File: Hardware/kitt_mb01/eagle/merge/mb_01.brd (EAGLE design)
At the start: 160 x 100 mm, 98 parts, among them CON1 ARDUINO_UNO, IC1.01 RT8293A, IC2.00 BQ24266RGET, IC3.01 LSM9DS1, P2 S2B-PH-K-S(LF)(SN), U6.01 TPS61032RSARPSDO-G16

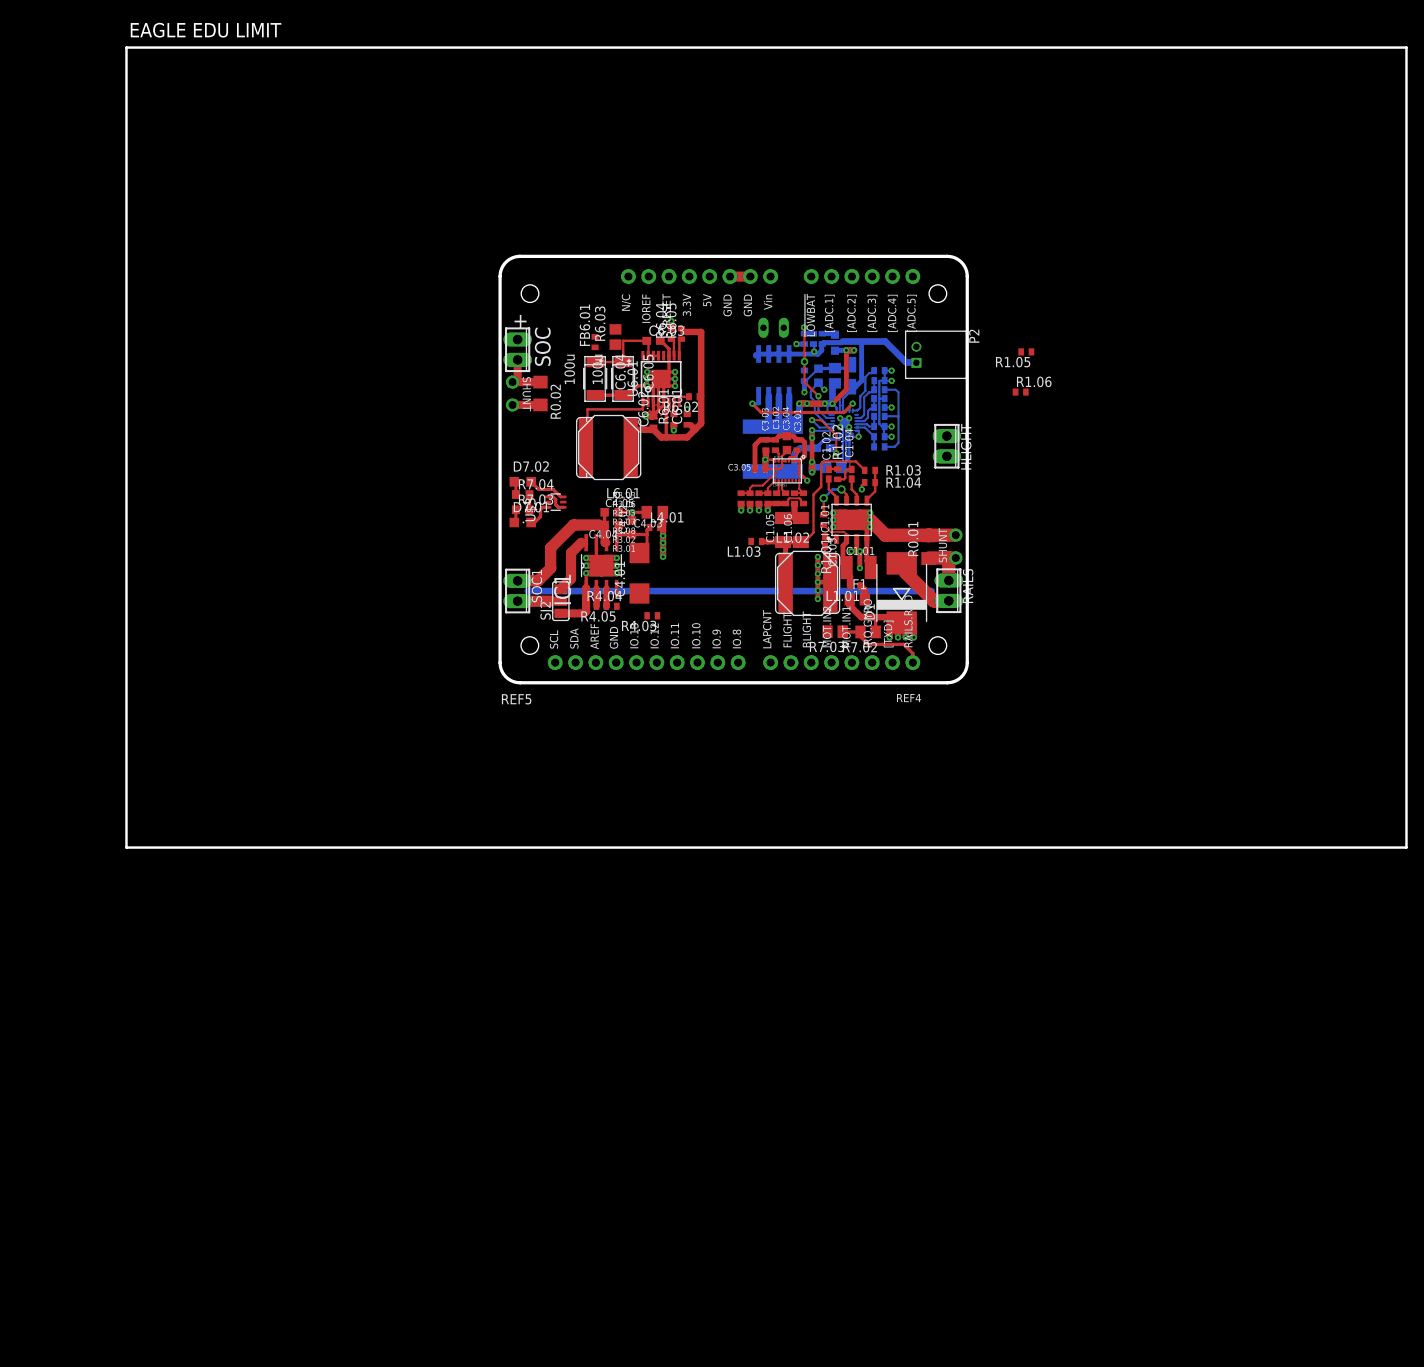
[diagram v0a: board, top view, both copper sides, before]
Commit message: snapshot of board merge
a point about the flipped LEDs with a hole:
it's mounted in reverse with a hole as a makeshift lightguard,
...because maybe.
There are actual LEDs with an lens attached (see knightbright),
but regular ones work as well obviously.
Also it allows for text to be silk'd right next to it, which is sweet.
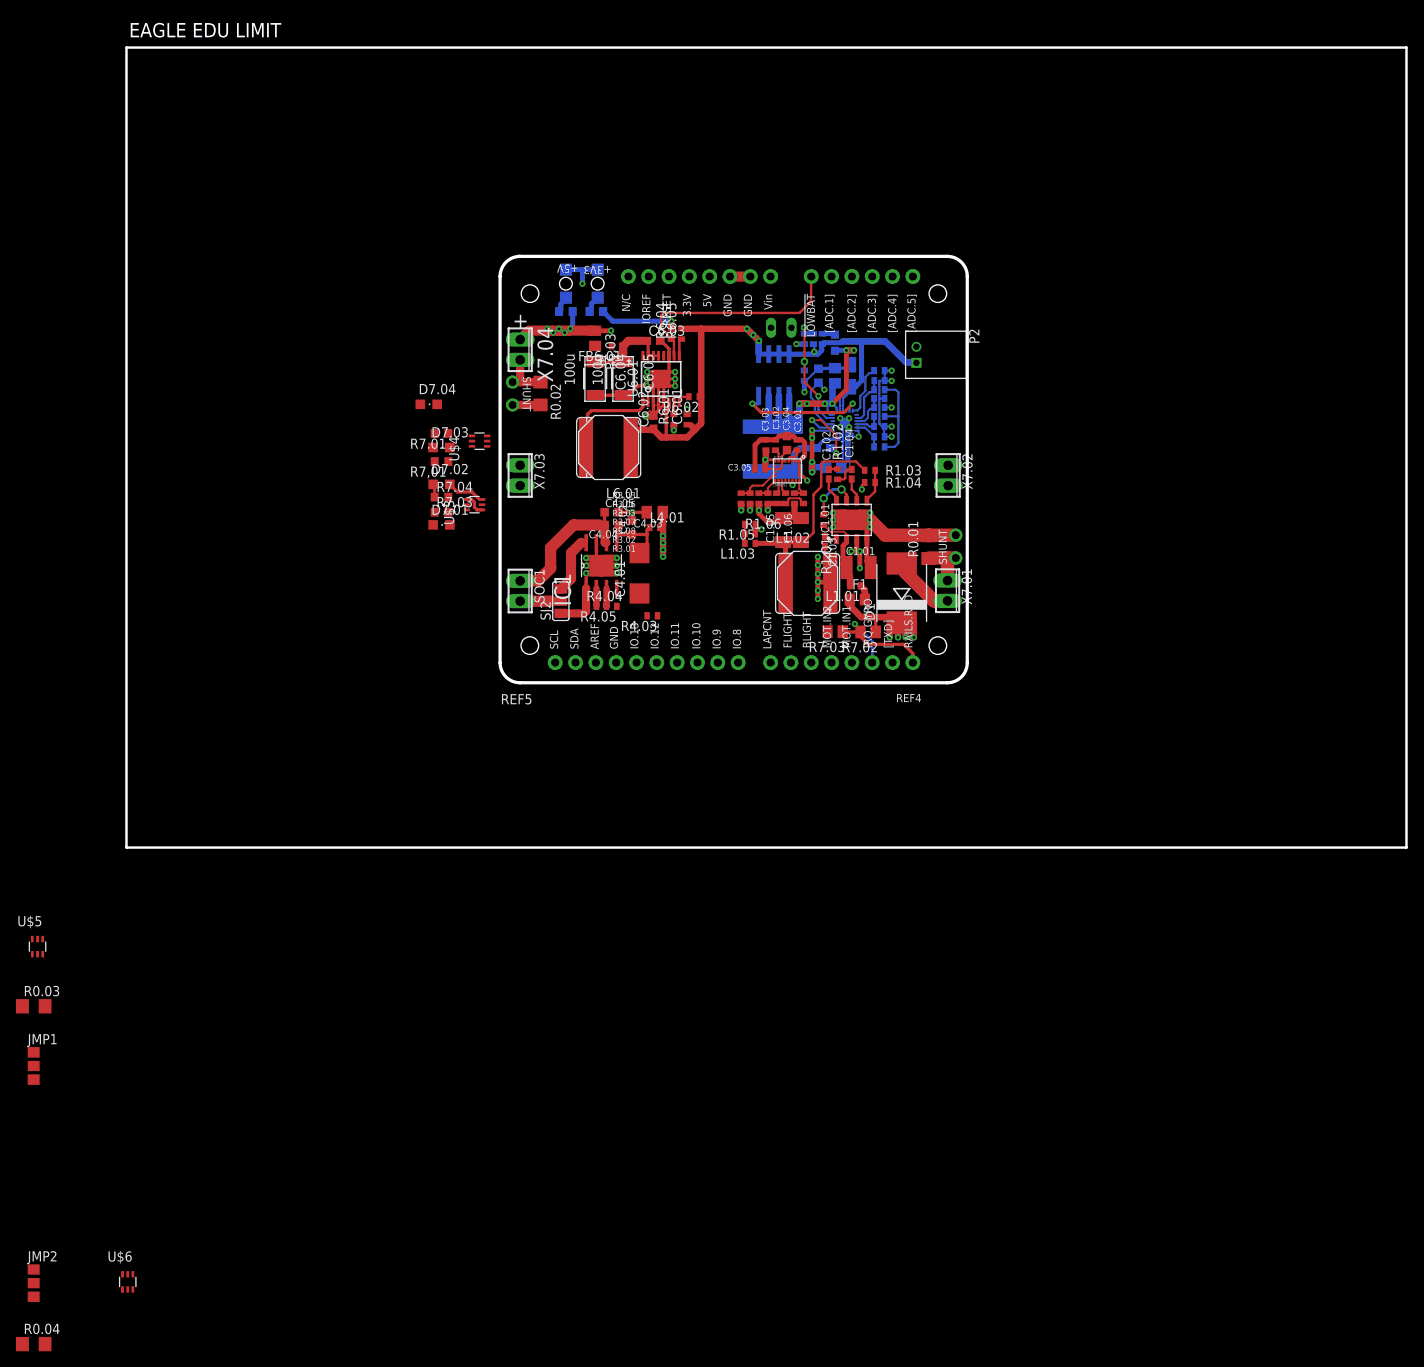
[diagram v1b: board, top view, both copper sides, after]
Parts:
- removed HLIGHT, RAILS, SOC: (no value), con-phoenix-254:2POL254
- added D7.03, D7.04: (no value), led:CHIPLED_0805
- added D7.05: OK+5V, led:CHIPLED_1206
- added D7.06: OK+3V, led:CHIPLED_1206
- added JMP1, JMP2: 0R-JUMPA, jump-0r-smd:A0R-JMP
- added R0.03, R0.04: [0R], rcl:R1206
- added R7,01, R7,02, R7,04, R7.01: 330R, rcl:R0603
- added U$4, U$5, U$6: SI1922EDH, kitt.ic:SC70-6
- added X7.01, X7.04: (no value), con-phoenix-254:2POL254
- added X7.02: HEAD-LIGHT, con-phoenix-254:2POL254
- added X7.03: TAIL-LIGHT, con-phoenix-254:2POL254
- moved R1.05 40.7 mm to (77.9, 40.4)
- moved R1.06 38.2 mm to (77.9, 39.2)
- moved D7.01 10.2 mm to (39.4, 40.3)
- moved D7.02 10.2 mm to (39.4, 45.4)
- moved R7,03 10.2 mm to (39.4, 41.9)
- moved R7.04 10.2 mm to (39.4, 43.8)
- moved U$3 10.2 mm to (43.5, 42.9)
- moved FB6.01 2.74 mm to (61.3, 62.7), turned to 180 degrees
- moved R6.03 2.54 mm to (58.6, 63.7), turned to 270 degrees
- moved R2.06 0.95 mm to (81.8, 65.0)
- moved L1.03 0.83 mm to (77.9, 38.0)
- moved SOC1 0.32 mm to (49.2, 32.1)
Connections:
- new net N$28: D7.03.C, U$4.6
- new net N$29: D7.03.A, R7,01.1
- new net N$30: D7.04.A, R7.01.1
- new net N$31: D7.04.C, U$4.3
- new net N$32: D7.05.A, R7,02.1
- new net N$38: D7.06.A, R7,04.1
- new net N$42: R0.03.2, X7.02.2
- new net N$44: R0.03.1, U$5.3
- new net N$45: JMP1.2, X7.02.1
- new net N$46: R0.04.2, X7.03.2
- new net N$47: R0.04.1, U$6.3
- new net N$48: JMP2.2, X7.03.1
- net +3V3: now also JMP1.1, JMP2.1, R7,01.2, R7,04.2, R7.01.2
- net +5V: now also JMP1.3, JMP2.3, R7,02.2, X7.04.1; no longer SOC.1
- net GND: now also D7.05.C, D7.06.C, U$4.1, U$4.4, U$5.4, U$6.4
- net GNDA: now also X7.01.1; no longer RAILS.1
- net N$25: now also X7.04.2; no longer SOC.2
- net VCC/2: now also X7.01.2; no longer RAILS.2
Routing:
- net +5V: track 9.63 -> 88.5 mm, vias 2 -> 9
- net N$2: track 50.5 -> 0.00 mm
- net !IRQ_GYRO: track 0.00 -> 44.1 mm, vias 0 -> 2
- net +3V3: track 39.1 -> 66.4 mm
- net LBO: track 2.44 -> 28.5 mm
- net +4.1V: track 83.1 -> 94.0 mm, vias 0 -> 3
- net GND: track 192.6 -> 202.4 mm, vias 38 -> 39
- net N$3: track 3.41 -> 0.44 mm
- net N$90: track 0.00 -> 2.38 mm
- net N$38: track 0.00 -> 2.16 mm
- net N$32: track 0.00 -> 2.09 mm
- net N$4: track 2.11 -> 0.52 mm
- net N$87: track 27.4 -> 28.3 mm
- net N$39: track 13.4 -> 12.8 mm
- net N$43: track 12.5 -> 11.9 mm
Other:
- board text added: "+3V3"
- board text added: "+5V"

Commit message: snapshot of board merge - added possible port expander via i2c - did some more routing - connected battery indicator leds
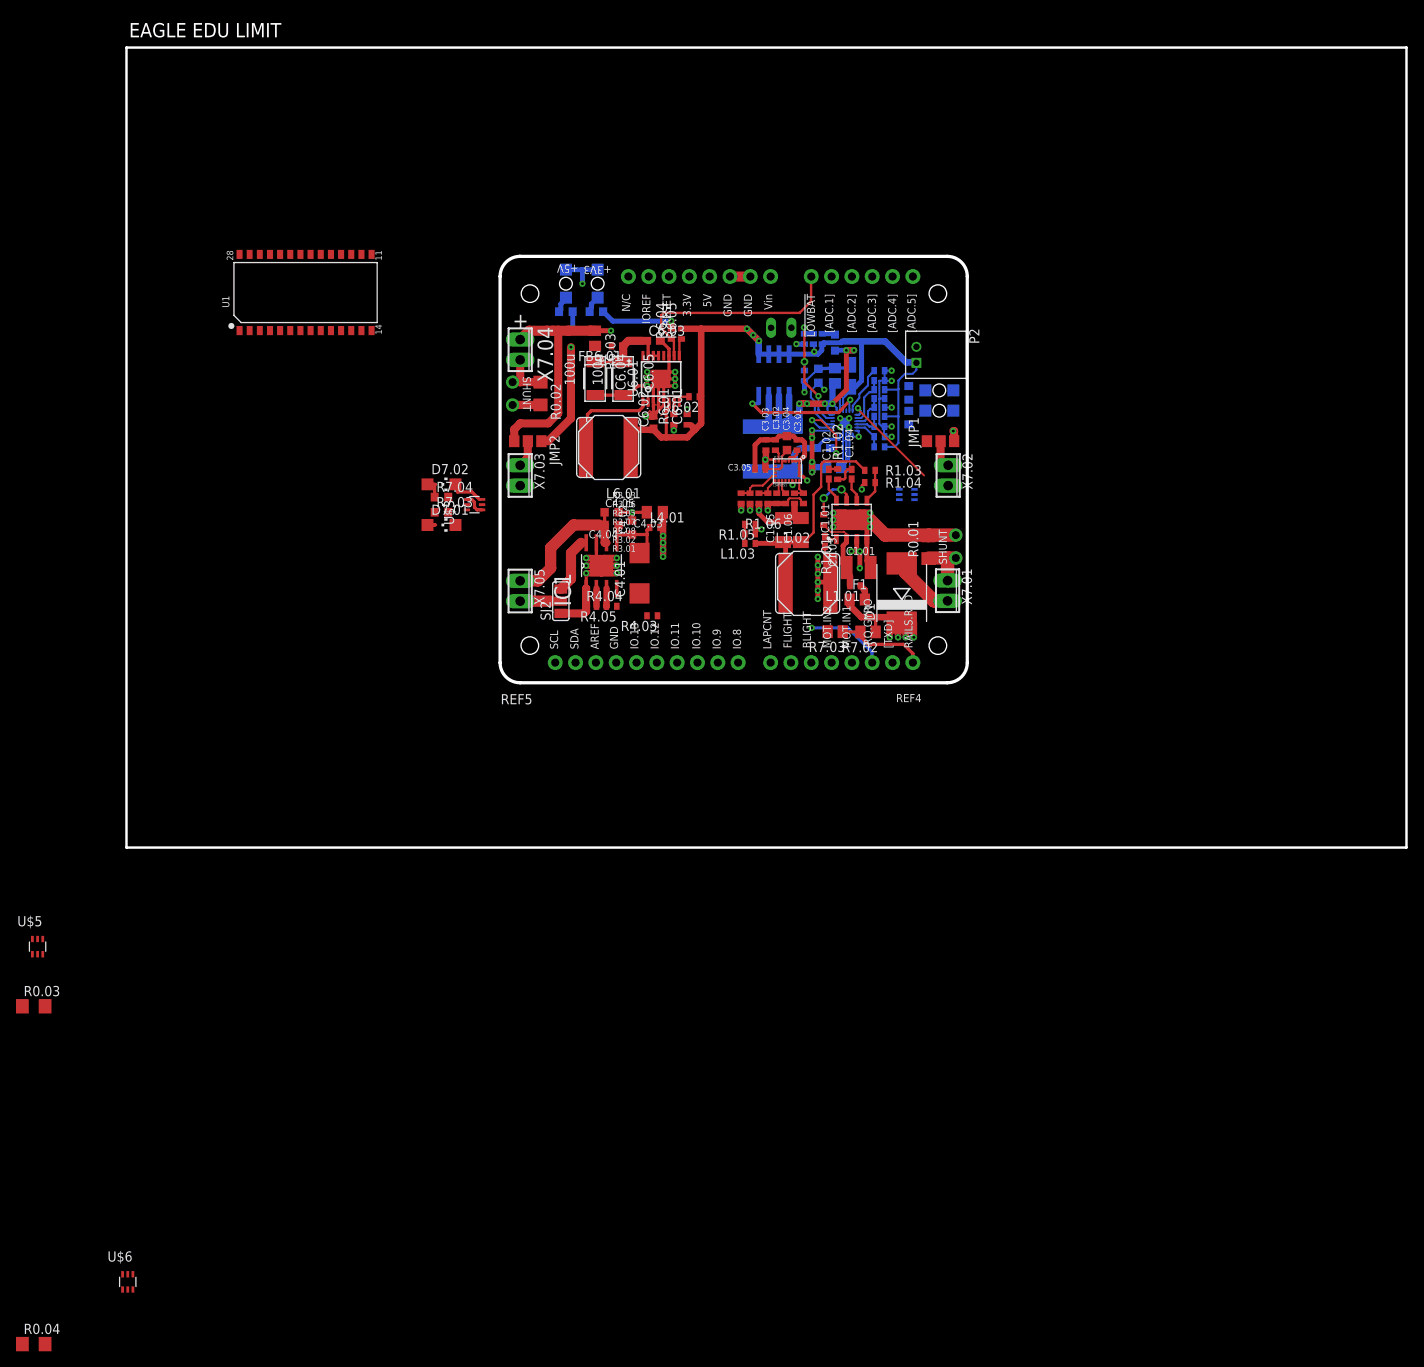
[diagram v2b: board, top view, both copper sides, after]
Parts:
- added U1: MCP23017-E, kitt.ic:SOIC28-1.27-17.9X7.5MM
- D7.01, D7.02, D7.03, D7.04: device led:CHIPLED_0805 -> led:CHIPLED_1206
- X7.05: value (none) -> MOTOR
- moved JMP1 137.7 mm to (101.8, 50.8), turned to 90 degrees
- moved JMP2 122.0 mm to (50.2, 50.8), turned to 270 degrees
- moved D7.04 63.8 mm to (101.6, 57.1), flipped to the bottom, turned to 90 degrees
- moved D7.03 62.4 mm to (101.6, 54.6), flipped to the bottom, turned to 90 degrees
- moved R7,01 58.7 mm to (97.8, 53.7), flipped to the bottom, turned to 90 degrees
- moved R7.01 58.6 mm to (97.8, 56.8), flipped to the bottom, turned to 270 degrees
- moved U$4 53.8 mm to (97.6, 44.1), flipped to the bottom
- renumbered SOC1 to X7.05
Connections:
- net IC2.0.!CHG: now also U$4.2
- net IC2.0.!PG: now also U$4.5
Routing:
- net +5V: track 88.5 -> 137.6 mm, vias 9 -> 5
- net +3V3: track 66.4 -> 84.0 mm, vias 4 -> 5
- net IC2.0.!CHG: track 0.00 -> 13.2 mm, vias 0 -> 1
- net !IRQ_GYRO: track 44.1 -> 37.5 mm
- net +4.1V: track 94.0 -> 99.1 mm
- net N$45: track 0.00 -> 3.97 mm
- net N$48: track 0.00 -> 3.41 mm
- net N$5: track 2.11 -> 3.51 mm
- net N$4: track 0.52 -> 1.92 mm
- net N$19: track 6.61 -> 6.11 mm

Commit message: snapshot of board merge  - it's going somewhere edition -
-> connected and routed head lights
-> did some power routing
-> next up: tail light
-> next² up: need for speedboards
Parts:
- removed U$5: SI1922EDH, kitt.ic:SC70-6
- added U7.01: SI1922EDH, kitt.ic:SC70-6
- moved R0.03 128.8 mm to (101.3, 42.2), flipped to the bottom, turned to 180 degrees
- moved U$3 25.5 mm to (18.2, 45.6)
- moved D7.01 25.5 mm to (14.0, 43.1)
- moved D7.02 25.5 mm to (14.0, 48.2)
- moved R7,03 25.5 mm to (14.0, 44.7)
- moved R7.04 25.5 mm to (14.0, 46.6)
- moved U$4 6.48 mm to (98.8, 50.5)
- moved L2.02 0.95 mm to (88.6, 64.1)
- moved R2.06 0.95 mm to (81.8, 65.9)
- moved C2.02 0.95 mm to (86.5, 59.9)
- moved C2.04 0.95 mm to (88.6, 59.9)
- moved C2.05 0.95 mm to (90.5, 59.9)
- moved R2.04 0.95 mm to (85.9, 64.5)
- moved R2.05 0.95 mm to (84.7, 59.9)
- moved R2.07 0.95 mm to (87.0, 64.5)
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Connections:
- removed net N$44: R0.03.1, U$5.3
- new net CAR.BLIGHT: CON1.IO.5
- new net CAR.FLIGHT: CON1.IO.6, U7.01.2
- new net CAR.LAPCNT: CON1.IO.7
- new net N$2: R0.03.1, U7.01.6
- net GND: now also U7.01.1; no longer U$5.4
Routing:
- net +3V3: track 84.0 -> 132.8 mm, vias 5 -> 10
- net CAR.FLIGHT: track 0.00 -> 35.6 mm
- net GND: track 202.4 -> 221.4 mm, vias 39 -> 44
- net IC2.0.!PG: track 0.00 -> 18.3 mm, vias 0 -> 2
- net N$31: track 0.00 -> 14.0 mm, vias 0 -> 2
- net N$28: track 0.00 -> 6.95 mm
- net +4.1V: track 99.1 -> 93.4 mm
- net N$29: track 0.00 -> 3.47 mm
- net N$42: track 0.00 -> 3.02 mm
- net N$2: track 0.00 -> 2.92 mm
- net N$30: track 0.00 -> 2.64 mm
- net IC2.0.!CHG: track 13.2 -> 10.7 mm, vias 1 -> 2
- net N$14: track 16.7 -> 18.9 mm
- net N$15: track 16.3 -> 18.5 mm
- net +5V: track 137.6 -> 139.3 mm
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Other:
- board text added: "<-- Battery Pak"
- board text added: "<-- Head Light"
- board text added: "SoC Supply -->"
- board text added: "Tail Light -->"
